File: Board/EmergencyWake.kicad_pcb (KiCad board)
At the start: 2 copper layers, 100 x 67 mm, 127 parts, among them J1 USB_C_Plug_USB2.0, J2 Micro_SD_Card_Det, J3 Conn_01x03, J4 Conn_01x02, J5 Conn_01x03, J6 Conn_01x04, J7 Conn_01x02, J8 Conn_01x04, J9 Conn_01x04, Q1 AO3400A, Q2 AO3401A, SW1 SW_DPDT_x2, SW2 SW_Push, SW3 SW_Push, SW4 SW_Push, U1 M24C02-WMN, U10 L9110S, U2 AMS1117-3.3, U3 MC34063AD, U4 STM32F103VETx, U5 LM4670, U6 AMS1117-3.3, U7 PT6312B, U8 EL357N-G, U9 EL357N-G, Y1 32,768

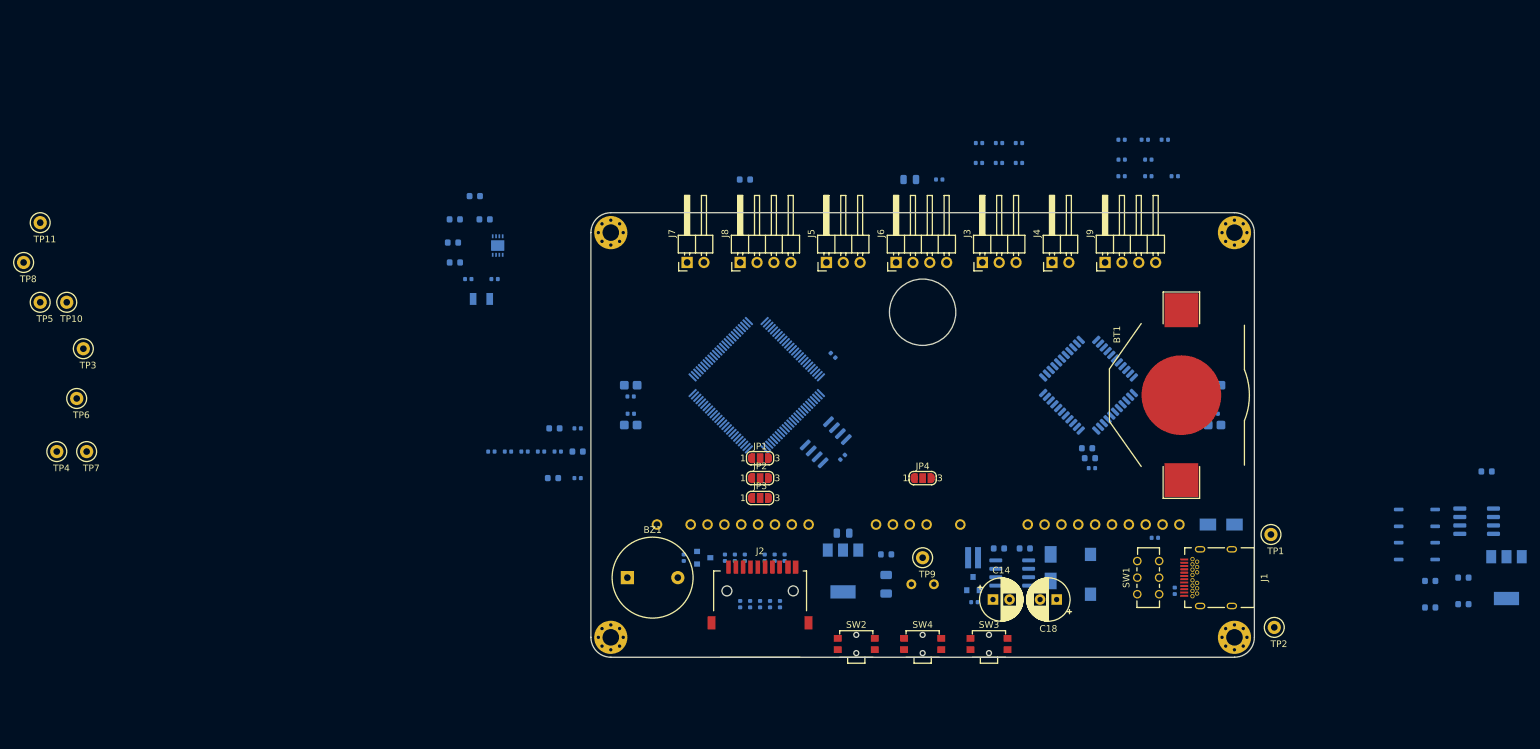
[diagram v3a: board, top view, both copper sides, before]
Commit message: [Board] Placed most components, only TPs missing
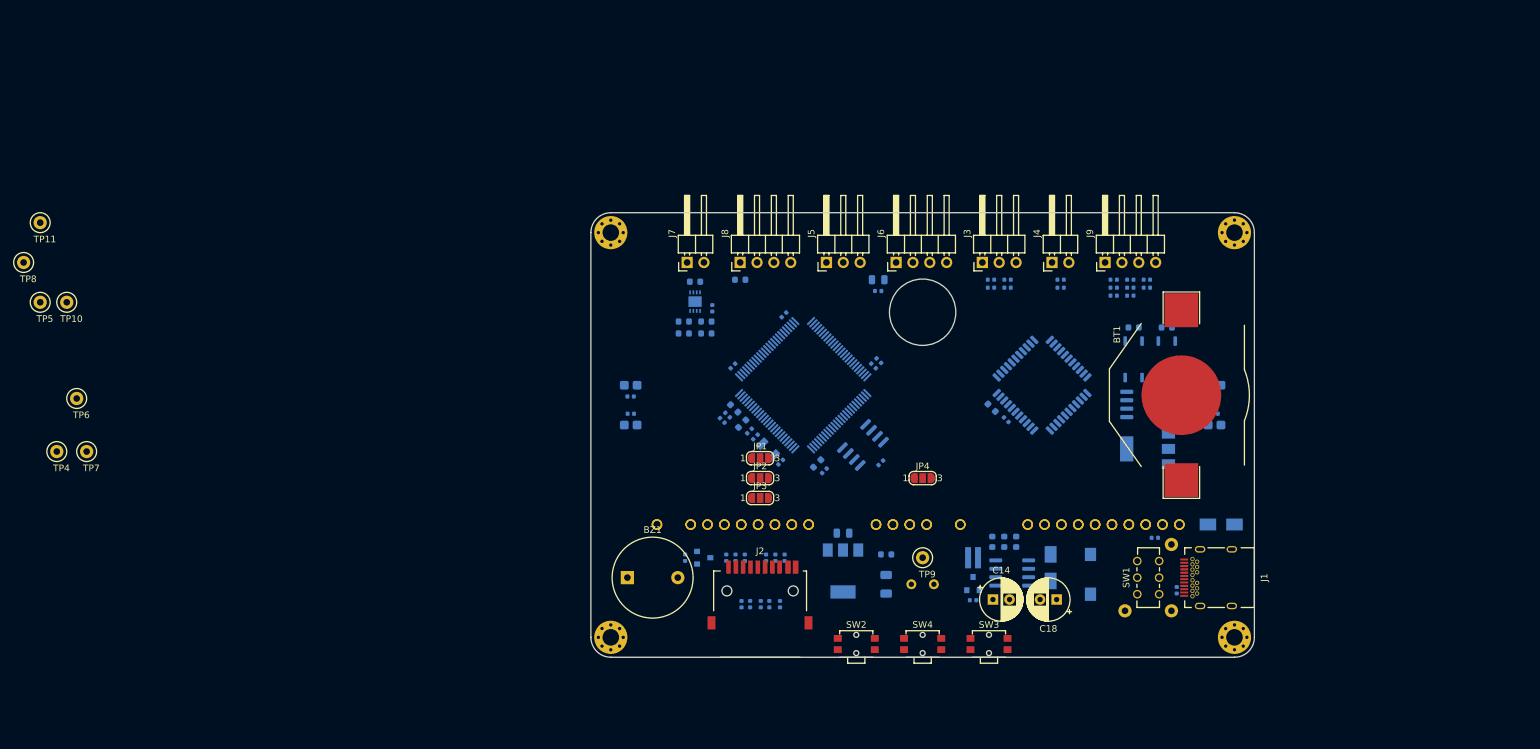
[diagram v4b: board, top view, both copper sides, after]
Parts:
- added DISP1: FUTABA_4-LT-46ZB3, VFD:FUTABA_4-LT-46ZB3, B.Cu at (150.0, 126.0)
- added R41: 100k, Resistor_SMD:R_0402_1005Metric, B.Cu at (118.3, 114.4)
- TP1, TP2, TP3: moved to B.Cu
- moved TP3 161.9 mm to (180.5, 160.0)
- moved R36 61.5 mm to (181.8, 117.3), turned to 180 degrees
- moved C7 59.0 mm to (142.6, 123.1), turned to 135 degrees
- moved U6 57.5 mm to (183.9, 135.6), turned to 180 degrees
- moved R35 55.1 mm to (186.8, 117.3), turned to 180 degrees
- moved R39 53.3 mm to (188.1, 128.0), turned to 270 degrees
- moved U10 53.2 mm to (183.3, 128.9)
- moved C22 51.2 mm to (128.6, 137.6), turned to 225 degrees
- moved R38 49.6 mm to (189.9, 128.0), turned to 270 degrees
- moved C21 49.4 mm to (124.8, 133.8), turned to 225 degrees
- moved U9 48.9 mm to (181.8, 122.1), turned to 270 degrees
- moved Y1 48.8 mm to (126.7, 135.7), turned to 135 degrees
- moved U8 47.5 mm to (186.8, 122.1), turned to 270 degrees
- moved C25 46.8 mm to (189.0, 130.6), turned to 180 degrees
- moved C6 46.4 mm to (129.1, 115.4), turned to 225 degrees
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
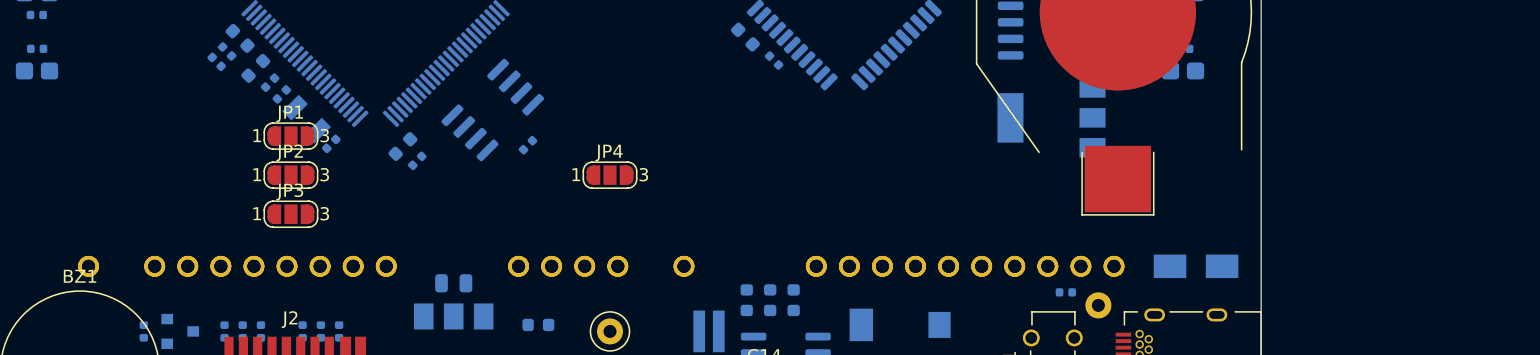
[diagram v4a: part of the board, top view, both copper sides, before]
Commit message: [Board] Changed lever to active high, replaced LDO for filament
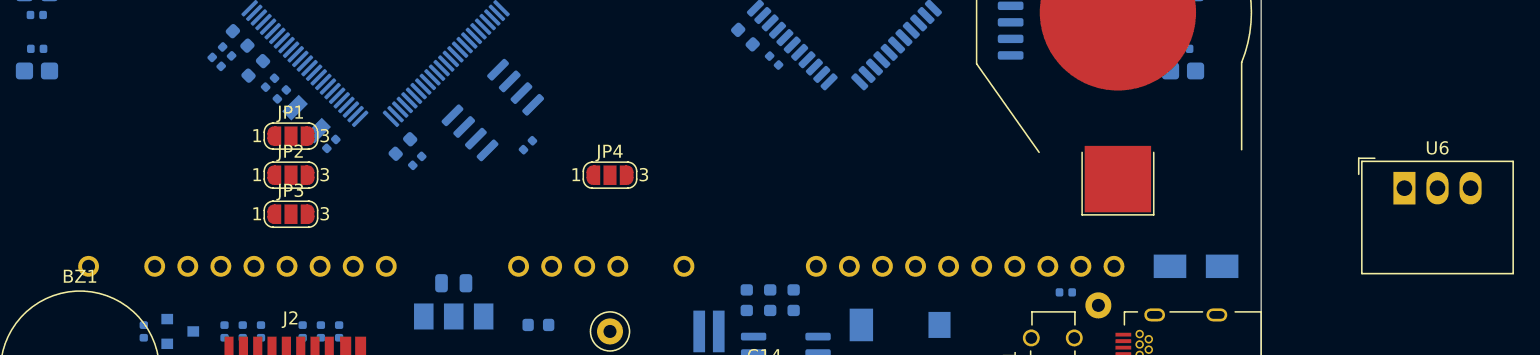
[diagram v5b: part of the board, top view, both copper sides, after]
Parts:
- removed the DISP1 at (150.0, 126.0)
- U6: value AMS1117-3.3 -> 173950378; footprint Package_TO_SOT_SMD:SOT-223-3_TabPin2 -> Converter_DCDC:Converter_DCDC_RECOM_R-78B-2.0_THT; moved to F.Cu
- moved U6 27.6 mm to (211.0, 141.0), turned to 0 degrees
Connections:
- J4 pad 2: GND -> VCC
- R30 pad 2: VCC -> GND
- U6 pad 1: -VDC -> GND
- U6 pad 2: Vdrive -> -VDC
- U6 pad 3: GND -> Vdrive
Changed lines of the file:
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@@
-(kicad_pcb (version 20171130) (host pcbnew "(5.1.4)-1")
+(kicad_pcb (version 20171130) (host pcbnew 5.1.5-52549c5~84~ubuntu16.04.1)
   (general
     (thickness 1.6)
@@
     (tracks 0)
     (zones 0)
-    (modules 129)
+    (modules 128)
     (nets 163)
   )
@@
     (diff_pair_gap 0.15)
   )
+  (module Converter_DCDC:Converter_DCDC_RECOM_R-78B-2.0_THT (layer F.Cu)
+    (at 211 141)
+    (descr "DCDC-Converter, RECOM, RECOM_R-78B-2.0, SIP-3, pitch 2.54mm, package size 11.5x8.5x17.5mm^3, https://www.recom-power.com/pdf/Innoline/R-78Bxx-2.0.pdf")
+    (tags "dc-dc recom buck sip-3 pitch 2.54mm")
+    (fp_text reference U6 (at 2.54 -3.06) (layer F.SilkS)
+      (effects (font (size 1 1) (thickness 0.15)))
+    )
+    (fp_text value 173950378 (at 2.54 7.5) (layer F.Fab)
+      (effects (font (size 1 1) (thickness 0.15)))
+    )
+    (fp_text user %R (at 2.54 2.25) (layer F.Fab)
+      (effects (font (size 1 1) (thickness 0.15)))
+    )
+    (fp_line (start 8.54 -2.25) (end -3.46 -2.25) (layer F.CrtYd) (width 0.05))
+    (fp_line (start 8.54 6.75) (end 8.54 -2.25) (layer F.CrtYd) (width 0.05))
+    (fp_line (start -3.46 6.75) (end 8.54 6.75) (layer F.CrtYd) (width 0.05))
+    (fp_line (start -3.46 -2.25) (end -3.46 6.75) (layer F.CrtYd) (width 0.05))
+    (fp_line (start -3.51 -2.3) (end -2.27 -2.3) (layer F.SilkS) (width 0.12))
+    (fp_line (start -3.51 -1.06) (end -3.51 -2.3) (layer F.SilkS) (width 0.12))
+    (fp_line (start 8.35 -2.06) (end 8.35 6.56) (layer F.SilkS) (width 0.12))
+    (fp_line (start -3.27 -2.06) (end -3.27 6.56) (layer F.SilkS) (width 0.12))
+    (fp_line (start -3.27 6.56) (end 8.35 6.56) (layer F.SilkS) (width 0.12))
+    (fp_line (start -3.27 -2.06) (end 8.35 -2.06) (layer F.SilkS) (width 0.12))
+    (fp_line (start -3.21 -1) (end -2.21 -2) (layer F.Fab) (width 0.1))
+    (fp_line (start -3.21 6.5) (end -3.21 -1) (layer F.Fab) (width 0.1))
+    (fp_line (start 8.29 6.5) (end -3.21 6.5) (layer F.Fab) (width 0.1))
+    (fp_line (start 8.29 -2) (end 8.29 6.5) (layer F.Fab) (width 0.1))
+    (fp_line (start -2.21 -2) (end 8.29 -2) (layer F.Fab) (width 0.1))
+    (pad 3 thru_hole oval (at 5.08 0) (size 1.7 2.5) (drill 1.2) (layers *.Cu *.Mask)
+      (net 59 Vdrive))
+    (pad 2 thru_hole oval (at 2.54 0) (size 1.7 2.5) (drill 1.2) (layers *.Cu *.Mask)
+      (net 55 -VDC))
+    (pad 1 thru_hole rect (at 0 0) (size 1.7 2.5) (drill 1.2) (layers *.Cu *.Mask)
+      (net 4 GND))
+    (model ${KISYS3DMOD}/Converter_DCDC.3dshapes/Converter_DCDC_RECOM_R-78B-2.0_THT.wrl
+      (at (xyz 0 0 0))
+      (scale (xyz 1 1 0.7))
+      (rotate (xyz 0 0 0))
+    )
+  )
   (module VFD:FUTABA_4-LT-46ZB3 locked (layer B.Cu)
     (at 150 126 180)
@@
     )
   )
-  (module Package_TO_SOT_SMD:SOT-223-3_TabPin2 (layer B.Cu)
-    (at 183.9 135.6 180)
-    (descr "module CMS SOT223 4 pins")
-    (tags "CMS SOT")
-    (attr smd)
-    (fp_text reference U6 (at 0 4.5 180) (layer B.SilkS)
-      (effects (font (size 1 1) (thickness 0.15)) (justify mirror))
-    )
-    (fp_text value AMS1117-3.3 (at 0 -4.5 180) (layer B.Fab)
-      (effects (font (size 1 1) (thickness 0.15)) (justify mirror))
-    )
-    (fp_line (start 1.85 3.35) (end 1.85 -3.35) (layer B.Fab) (width 0.1))
-    (fp_line (start -1.85 -3.35) (end 1.85 -3.35) (layer B.Fab) (width 0.1))
-    (fp_line (start -4.1 3.41) (end 1.91 3.41) (layer B.SilkS) (width 0.12))
-    (fp_line (start -0.85 3.35) (end 1.85 3.35) (layer B.Fab) (width 0.1))
-    (fp_line (start -1.85 -3.41) (end 1.91 -3.41) (layer B.SilkS) (width 0.12))
-    (fp_line (start -1.85 2.35) (end -1.85 -3.35) (layer B.Fab) (width 0.1))
-    (fp_line (start -1.85 2.35) (end -0.85 3.35) (layer B.Fab) (width 0.1))
-    (fp_line (start -4.4 3.6) (end -4.4 -3.6) (layer B.CrtYd) (width 0.05))
-    (fp_line (start -4.4 -3.6) (end 4.4 -3.6) (layer B.CrtYd) (width 0.05))
-    (fp_line (start 4.4 -3.6) (end 4.4 3.6) (layer B.CrtYd) (width 0.05))
-    (fp_line (start 4.4 3.6) (end -4.4 3.6) (layer B.CrtYd) (width 0.05))
-    (fp_line (start 1.91 3.41) (end 1.91 2.15) (layer B.SilkS) (width 0.12))
-    (fp_line (start 1.91 -3.41) (end 1.91 -2.15) (layer B.SilkS) (width 0.12))
-    (fp_text user %R (at 0 0 90) (layer B.Fab)
-      (effects (font (size 0.8 0.8) (thickness 0.12)) (justify mirror))
-    )
-    (pad 1 smd rect (at -3.15 2.3 180) (size 2 1.5) (layers B.Cu B.Paste B.Mask)
-      (net 55 -VDC))
-    (pad 3 smd rect (at -3.15 -2.3 180) (size 2 1.5) (layers B.Cu B.Paste B.Mask)
-      (net 4 GND))
-    (pad 2 smd rect (at -3.15 0 180) (size 2 1.5) (layers B.Cu B.Paste B.Mask)
-      (net 59 Vdrive))
-    (pad 2 smd rect (at 3.15 0 180) (size 2 3.8) (layers B.Cu B.Paste B.Mask)
-      (net 59 Vdrive))
-    (model ${KISYS3DMOD}/Package_TO_SOT_SMD.3dshapes/SOT-223.wrl
-      (at (xyz 0 0 0))
-      (scale (xyz 1 1 1))
-      (rotate (xyz 0 0 0))
-    )
-  )
   (module Package_SON:WSON-8-1EP_3x3mm_P0.5mm_EP1.6x2.0mm (layer B.Cu)
     (at 115.7 113.4 90)
@@
     (fp_line (start -0.5 -0.25) (end -0.5 0.25) (layer B.Fab) (width 0.1))
     (pad 2 smd roundrect (at 0.485 0) (size 0.59 0.64) (layers B.Cu B.Paste B.Mask) (roundrect_rratio 0.25)
-      (net 7 VCC))
+      (net 4 GND))
     (pad 1 smd roundrect (at -0.485 0) (size 0.59 0.64) (layers B.Cu B.Paste B.Mask) (roundrect_rratio 0.25)
       (net 12 /LEVER))
@@
     (model ${KISYS3DMOD}/Capacitor_THT.3dshapes/CP_Radial_D6.3mm_P2.50mm.wrl
       (at (xyz 0 0 0))
-      (scale (xyz 1 1 1))
+      (scale (xyz 1 1 1.8))
       (rotate (xyz 0 0 0))
     )
@@
     (model ${KISYS3DMOD}/Capacitor_THT.3dshapes/CP_Radial_D6.3mm_P2.50mm.wrl
       (at (xyz 0 0 0))
-      (scale (xyz 1 1 1))
+      (scale (xyz 1 1 1.8))
       (rotate (xyz 0 0 0))
     )
@@
     )
   )
-  (module VFD:FUTABA_4-LT-46ZB3 locked (layer B.Cu)
-    (at 150 126 180)
-    (fp_text reference DISP1 (at 0 1.6) (layer B.SilkS)
-      (effects (font (size 1 1) (thickness 0.15)) (justify mirror))
-    )
-    (fp_text value FUTABA_4-LT-46ZB3 (at 0 0) (layer B.Fab)
-      (effects (font (size 1 1) (thickness 0.15)) (justify mirror))
-    )
-    (fp_line (start -40 -16.5) (end 40 -16.5) (layer B.SilkS) (width 0.15))
-    (fp_line (start -40 17) (end 40 17) (layer B.SilkS) (width 0.15))
-    (pad 32 thru_hole circle (at 40.04 -21 180) (size 1.6 1.6) (drill 1) (layers *.Cu *.Mask)
-      (net 17 "Net-(DISP1-Pad32)"))
-    (pad 30 thru_hole circle (at 34.96 -21 180) (size 1.6 1.6) (drill 1) (layers *.Cu *.Mask)
-      (net 18 "Net-(DISP1-Pad30)"))
-    (pad 29 thru_hole circle (at 32.42 -21 180) (size 1.6 1.6) (drill 1) (layers *.Cu *.Mask)
-      (net 19 /VFD_GRID_1_HV))
-    (pad 28 thru_hole circle (at 29.88 -21 180) (size 1.6 1.6) (drill 1) (layers *.Cu *.Mask)
-      (net 20 "Net-(DISP1-Pad28)"))
-    (pad 27 thru_hole circle (at 27.34 -21 180) (size 1.6 1.6) (drill 1) (layers *.Cu *.Mask)
-      (net 21 "Net-(DISP1-Pad27)"))
-    (pad 26 thru_hole circle (at 24.8 -21 180) (size 1.6 1.6) (drill 1) (layers *.Cu *.Mask)
-      (net 22 "Net-(DISP1-Pad26)"))
-    (pad 25 thru_hole circle (at 22.26 -21 180) (size 1.6 1.6) (drill 1) (layers *.Cu *.Mask)
-      (net 19 /VFD_GRID_1_HV))
-    (pad 24 thru_hole circle (at 19.72 -21 180) (size 1.6 1.6) (drill 1) (layers *.Cu *.Mask)
-      (net 23 "Net-(DISP1-Pad24)"))
-    (pad 23 thru_hole circle (at 17.18 -21 180) (size 1.6 1.6) (drill 1) (layers *.Cu *.Mask)
-      (net 24 /VFD_GRID_2_HV))
-    (pad 19 thru_hole circle (at 7.02 -21 180) (size 1.6 1.6) (drill 1) (layers *.Cu *.Mask)
-      (net 24 /VFD_GRID_2_HV))
-    (pad 18 thru_hole circle (at 4.48 -21 180) (size 1.6 1.6) (drill 1) (layers *.Cu *.Mask)
-      (net 25 "Net-(DISP1-Pad18)"))
-    (pad 17 thru_hole circle (at 1.94 -21 180) (size 1.6 1.6) (drill 1) (layers *.Cu *.Mask)
-      (net 26 "Net-(DISP1-Pad17)"))
-    (pad 16 thru_hole circle (at -0.6 -21 180) (size 1.6 1.6) (drill 1) (layers *.Cu *.Mask)
-      (net 27 "Net-(DISP1-Pad16)"))
-    (pad 14 thru_hole circle (at -5.68 -21 180) (size 1.6 1.6) (drill 1) (layers *.Cu *.Mask)
-      (net 28 /VFD_GRID_4_HV))
-    (pad 10 thru_hole circle (at -15.84 -21 180) (size 1.6 1.6) (drill 1) (layers *.Cu *.Mask)
-      (net 28 /VFD_GRID_4_HV))
-    (pad 9 thru_hole circle (at -18.38 -21 180) (size 1.6 1.6) (drill 1) (layers *.Cu *.Mask)
-      (net 66 /SEG_L))
-    (pad 8 thru_hole circle (at -20.92 -21 180) (size 1.6 1.6) (drill 1) (layers *.Cu *.Mask)
-      (net 29 /VFD_GRID_5_HV))
-    (pad 7 thru_hole circle (at -23.46 -21 180) (size 1.6 1.6) (drill 1) (layers *.Cu *.Mask)
-      (net 30 "Net-(DISP1-Pad7)"))
-    (pad 6 thru_hole circle (at -26 -21 180) (size 1.6 1.6) (drill 1) (layers *.Cu *.Mask)
-      (net 31 "Net-(DISP1-Pad6)"))
-    (pad 5 thru_hole circle (at -28.54 -21 180) (size 1.6 1.6) (drill 1) (layers *.Cu *.Mask)
-      (net 32 "Net-(DISP1-Pad5)"))
-    (pad 4 thru_hole circle (at -31.08 -21 180) (size 1.6 1.6) (drill 1) (layers *.Cu *.Mask)
-      (net 29 /VFD_GRID_5_HV))
-    (pad 3 thru_hole circle (at -33.62 -21 180) (size 1.6 1.6) (drill 1) (layers *.Cu *.Mask)
-      (net 33 "Net-(DISP1-Pad3)"))
-    (pad 2 thru_hole circle (at -36.16 -21 180) (size 1.6 1.6) (drill 1) (layers *.Cu *.Mask)
-      (net 34 "Net-(DISP1-Pad2)"))
-    (pad 1 thru_hole circle (at -38.7 -21 180) (size 1.6 1.6) (drill 1) (layers *.Cu *.Mask)
-      (net 35 "Net-(DISP1-Pad1)"))
-  )
   (module Capacitor_SMD:C_0402_1005Metric (layer B.Cu)
     (at 162.6 131.2 135)
@@
     (fp_line (start 2.135 -1.27) (end 4.04 -1.27) (layer F.Fab) (width 0.1))
     (pad 2 thru_hole oval (at 0 2.54 90) (size 1.7 1.7) (drill 1) (layers *.Cu *.Mask)
-      (net 4 GND))
+      (net 7 VCC))
     (pad 1 thru_hole rect (at 0 0 90) (size 1.7 1.7) (drill 1) (layers *.Cu *.Mask)
       (net 12 /LEVER))
